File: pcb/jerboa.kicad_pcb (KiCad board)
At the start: 2 copper layers, 53.6 x 134.2 mm, 89 parts, among them IC1 SL18860DC, IC2 MAX-M8Q, IC3 Si4460, J1 CONN_01x02, J2 CONN_01x03, J3 CONN_01x02, J4 CONN_01x02, P1 SWD_TC, P2 144MHz, P3 434MHz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

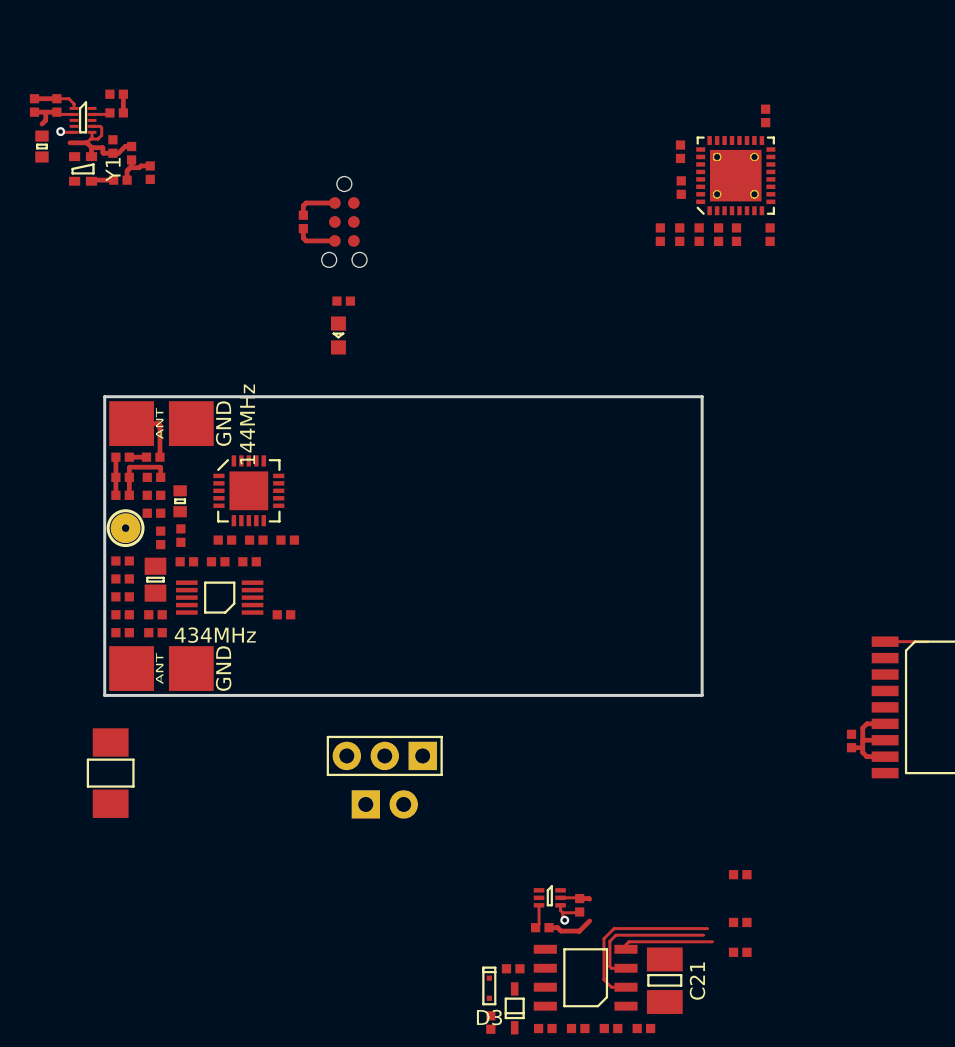
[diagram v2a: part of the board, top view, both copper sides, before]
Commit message: WIP: more pcb layout, add rx stuff again
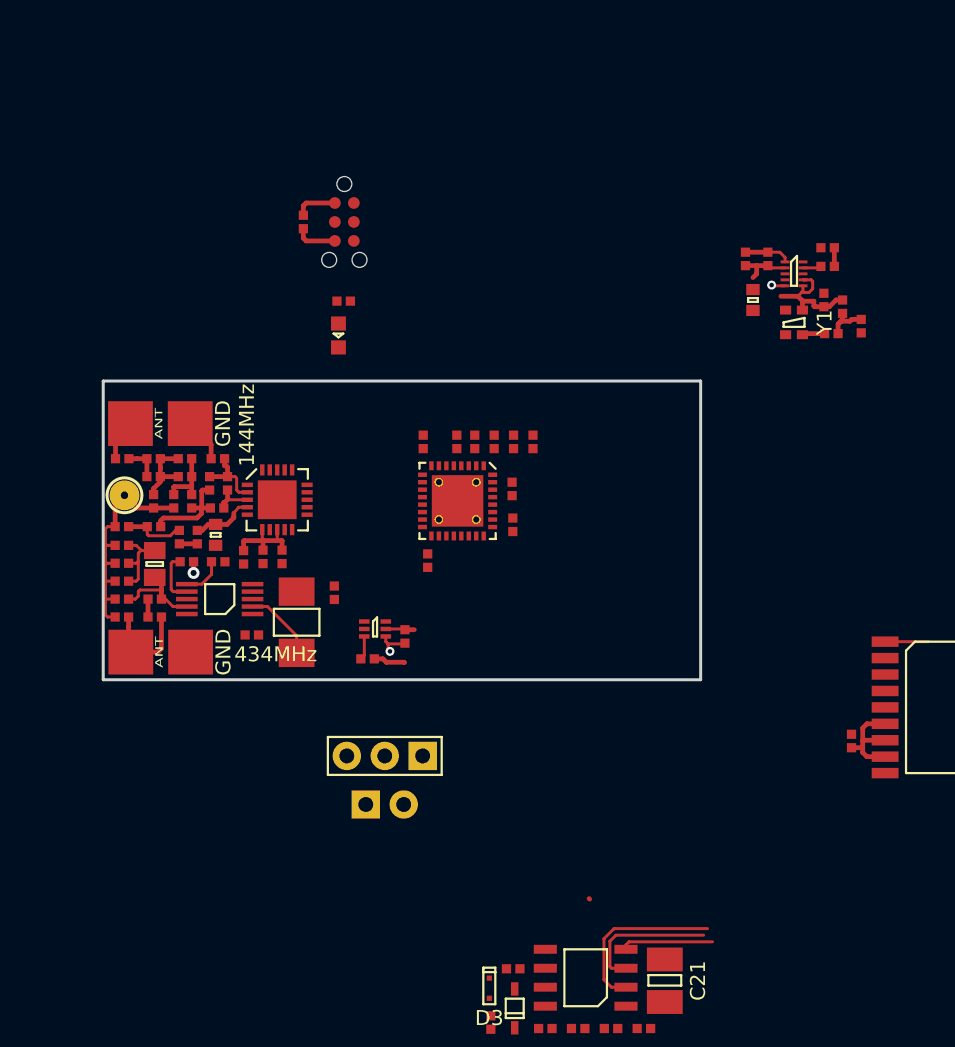
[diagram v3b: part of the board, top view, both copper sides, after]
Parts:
- added CR1: 12pF, agg:0402, F.Cu at (42.6, 84.2)
- added CR2: 6.2pF, agg:0402, F.Cu at (42.5, 87.5)
- added LR1: 220nH, agg:0402, F.Cu at (43.2, 85.8)
- added LR2: 150nH, agg:0402, F.Cu at (42.0, 85.8)
- moved CM3 49.5 mm to (38.3, 87.0), turned to 270 degrees
- moved CP2 49.3 mm to (38.3, 85.3), turned to 180 degrees
- moved C1 48.7 mm to (83.2, 73.5)
- moved C2 48.7 mm to (83.7, 75.8)
- moved C3 48.7 mm to (77.9, 70.8)
- moved C4 48.7 mm to (79.4, 70.8)
- moved IC1 48.7 mm to (81.2, 71.8)
- moved R1 48.7 mm to (84.4, 74.0)
- moved R2 48.7 mm to (85.7, 75.3)
- moved R3 48.7 mm to (78.4, 73.5)
- moved R4 48.7 mm to (83.4, 71.3)
- moved R5 48.7 mm to (83.4, 70.0)
- moved Y1 48.7 mm to (81.2, 75.0)
- moved CM2 45.4 mm to (39.6, 87.0), turned to 270 degrees
- moved C6 37.4 mm to (56.6, 91.0), turned to 90 degrees
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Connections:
- IC3 pad 2: /radio/RADIO_RXn -> /radio/RADIO_RXp
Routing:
- net GND: track 20.7 -> 40.2 mm, vias 2 -> 3
- net Net-(C30-Pad1): track 0.00 -> 8.33 mm
- net Net-(CR2-Pad2): track 0.00 -> 6.65 mm
- net Net-(C27-Pad2): track 0.00 -> 6.18 mm
- net Net-(C29-Pad1): track 0.00 -> 5.31 mm
- net 3v3: track 27.1 -> 32.1 mm
- net Net-(C22-Pad2): track 0.00 -> 4.91 mm
- net /radio/RADIO_RXp: track 0.00 -> 4.77 mm
- net /radio/RADIO_TX: track 0.00 -> 4.19 mm
- net Net-(CM1-Pad1): track 0.00 -> 4.10 mm
- net /MICRF_EN: track 0.00 -> 3.52 mm
- net Net-(R17-Pad1): track 0.00 -> 2.77 mm
- net /radio/RADIO_RXn: track 0.00 -> 2.67 mm
- net Net-(CM3-Pad1): track 2.55 -> 4.99 mm
- net Net-(CC2-Pad2): track 4.10 -> 2.76 mm
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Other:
- outline, holes or cut-outs redrawn

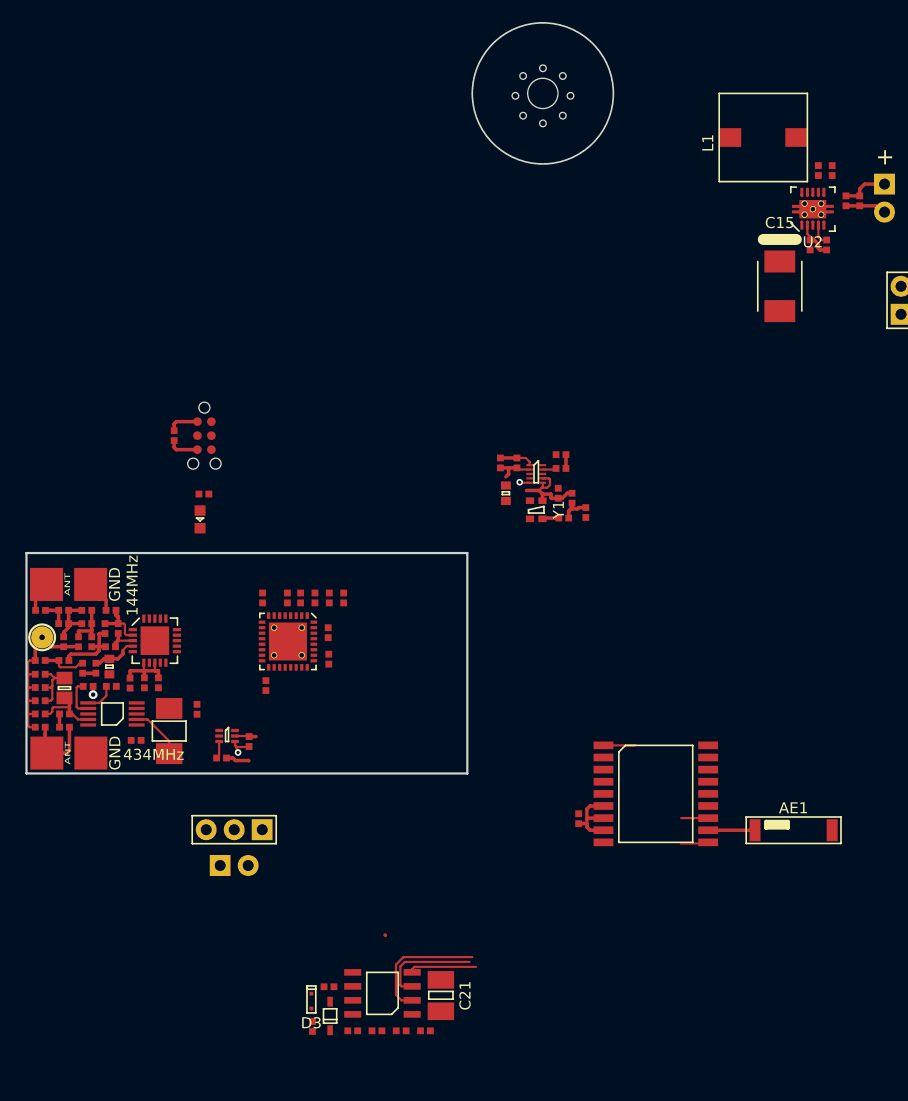
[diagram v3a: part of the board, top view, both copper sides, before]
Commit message: WIP: add clock circuitry to pcb
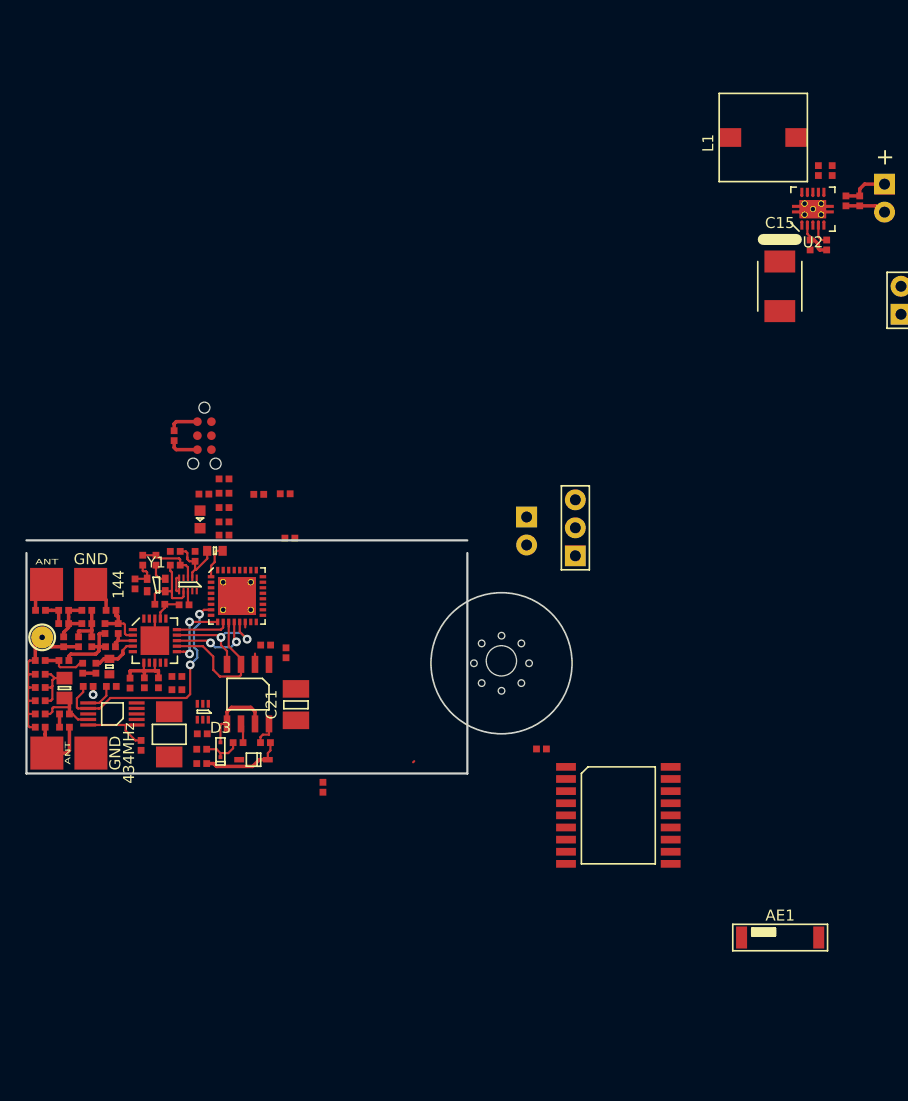
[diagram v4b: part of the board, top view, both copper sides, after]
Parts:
- P2: value 144MHz -> 144
- moved X1 51.6 mm to (78.0, 89.0)
- moved J2 41.3 mm to (84.7, 76.7), turned to 90 degrees
- moved J4 40.3 mm to (80.3, 77.0), turned to 270 degrees
- moved R1 39.4 mm to (45.5, 79.6), turned to 90 degrees
- moved C1 39.3 mm to (44.8, 81.8), turned to 90 degrees
- moved R5 38.8 mm to (47.0, 83.6)
- moved R2 37.6 mm to (48.4, 80.0), turned to 180 degrees
- moved C2 37.2 mm to (46.6, 79.6), turned to 90 degrees
- moved R13 37.1 mm to (56.6, 87.3)
- moved C20 36.6 mm to (58.5, 88.0), turned to 90 degrees
- moved R4 36.4 mm to (49.2, 83.7), turned to 180 degrees
- moved Y1 35.1 mm to (46.7, 81.8), turned to 0 degrees
- moved IC1 33.2 mm to (49.5, 81.8), turned to 270 degrees
- moved C3 30.6 mm to (48.4, 78.8), turned to 0 degrees
- moved C4 30.4 mm to (50.2, 79.2)
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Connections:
- IC1 pad 10: Net-(IC1-Pad10) -> /MCU_CLK
- IC1 pad 5: GND -> 3v3
- IC1 pad 7: 3v3 -> GND
- IC1 pad 8: /MCU_CLK -> Net-(IC1-Pad8)
- R4 pad 1: Net-(IC1-Pad9) -> Net-(IC1-Pad8)
- U1 pad 15: /MICRF_EN -> Net-(U1-Pad15)
- U1 pad 25: Net-(U1-Pad25) -> /LOW_BATT
- U1 pad 7: /LOW_BATT -> /MICRF_EN
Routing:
- net /MICRF_EN: track 3.52 -> 22.2 mm, vias 0 -> 2
- net /DAC_NCS: track 12.3 -> 1.47 mm
- net /MCU_MISO: track 0.00 -> 7.74 mm, vias 0 -> 2
- net Net-(C22-Pad1): track 0.00 -> 7.56 mm
- net /MCU_nIRQ_TO_RADIO: track 0.00 -> 6.70 mm, vias 0 -> 2
- net 3v3: track 32.1 -> 26.4 mm
- net Net-(C22-Pad2): track 4.91 -> 0.00 mm
- net /SI4460_NSS: track 0.00 -> 4.78 mm
- net /MCU_MOSI: track 6.65 -> 11.4 mm, vias 0 -> 2
- net Net-(AE1-Pad2): track 4.25 -> 0.00 mm
- net Net-(C23-Pad1): track 0.00 -> 3.61 mm
- net /MCU_SCK: track 9.74 -> 13.0 mm
- net Net-(C2-Pad2): track 2.99 -> 5.71 mm
- net GND: track 40.2 -> 42.7 mm, vias 3 -> 1
- net /radio/COARSE: track 0.00 -> 2.35 mm
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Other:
- board size 53.6 x 134.2 mm -> 49.8 x 87.2 mm

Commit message: WIP: attempt at routing spi
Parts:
- moved C6 32.1 mm to (54.8, 79.0), turned to 270 degrees
- moved C11 21.7 mm to (67.2, 78.9)
- moved R7 17.8 mm to (51.5, 90.8), turned to 90 degrees
- moved P1 16.4 mm to (63.0, 79.7), turned to 180 degrees
- moved IC2 16.0 mm to (101.2, 92.8)
- moved D1 15.2 mm to (49.7, 60.7)
- moved R6 15.2 mm to (50.0, 58.4)
- moved R9 15.1 mm to (44.9, 83.6), turned to 0 degrees
- moved C9 14.1 mm to (60.5, 85.3), turned to 180 degrees
- moved C7 11.6 mm to (51.4, 83.7)
- moved C8 7.72 mm to (51.4, 84.9)
- moved C10 6.45 mm to (51.9, 82.5)
- moved C5 4.30 mm to (53.6, 79.0), turned to 270 degrees
- moved U1 2.46 mm to (56.5, 83.0)
- moved R1 2.42 mm to (47.7, 80.5)
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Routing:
- net 3v3: track 26.4 -> 59.6 mm, vias 0 -> 2
- net /MCU_SHUTDOWN_TO_RADIO: track 0.00 -> 12.6 mm, vias 0 -> 2
- net /I2C_SCL: track 0.00 -> 11.6 mm
- net /I2C_SDA: track 0.00 -> 10.2 mm
- net /MCU_MOSI: track 11.4 -> 18.7 mm
- net /TMP_ALERT: track 0.07 -> 6.64 mm
- net /SWDIO: track 0.00 -> 6.13 mm
- net /MICRF_EN: track 22.2 -> 28.3 mm
- net /DAC_NCS: track 1.47 -> 7.02 mm
- net /SWCLK: track 0.00 -> 4.71 mm
- net Net-(C3-Pad2): track 5.88 -> 1.34 mm
- net /MCU_CLK: track 0.00 -> 4.18 mm
- net Net-(C24-Pad1): track 0.00 -> 2.70 mm
- net /SI4460_NSS: track 4.78 -> 7.43 mm
- net /MCU_SCK: track 13.0 -> 10.4 mm
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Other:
- board size 49.8 x 87.2 mm -> 49.8 x 87.5 mm

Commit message: WIP: more pcb layout
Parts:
- J3, J4: moved to F.Cu
- P2: value 144 -> 144MHz
- X1: footprint agg:M2.5_MOUNT -> agg:M2.5_HOLE
- moved J1 81.7 mm to (45.5, 100.2), turned to 0 degrees
- moved L1 54.0 mm to (68.1, 80.9), turned to 0 degrees
- moved J3 54.0 mm to (68.0, 76.9), turned to 180 degrees
- moved C13 53.1 mm to (67.0, 79.1), turned to 180 degrees
- moved C12 52.3 mm to (69.2, 79.1), turned to 0 degrees
- moved R10 50.3 mm to (73.3, 80.7), turned to 180 degrees
- moved R11 48.5 mm to (73.3, 79.4), turned to 0 degrees
- moved U2 47.6 mm to (74.6, 83.3), turned to 90 degrees
- moved R12 43.4 mm to (75.8, 80.7), turned to 180 degrees
- moved C14 41.5 mm to (75.8, 79.4), turned to 180 degrees
- moved C15 40.0 mm to (78.8, 84.2), turned to 180 degrees
- moved J2 37.9 mm to (46.8, 76.9), turned to 180 degrees
- moved IC2 33.0 mm to (68.2, 93.3)
- moved AE1 28.9 mm to (80.1, 96.7)
- moved J4 26.3 mm to (68.0, 100.2), turned to 0 degrees
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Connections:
- U1 pad 15: Net-(U1-Pad15) -> /SOLAR_CELL_VOLTAGE
- U1 pad 6: /SOLAR_CELL_VOLTAGE -> Net-(U1-Pad6)
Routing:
- net 3v3: track 59.6 -> 101.5 mm
- net Net-(C12-Pad1): track 4.31 -> 36.2 mm
- net /GPS_~RESET: track 0.00 -> 17.0 mm, vias 0 -> 2
- net GND: track 42.6 -> 59.1 mm, vias 3 -> 11
- net /TX_GPS_from_MCU: track 0.00 -> 10.8 mm
- net /RX_GPS_from_MCU: track 0.00 -> 10.2 mm
- net /I2C_SCL: track 11.6 -> 2.37 mm
- net /I2C_SDA: track 10.2 -> 2.77 mm
- net Net-(L1-Pad2): track 0.00 -> 6.18 mm
- net /SWDIO: track 6.13 -> 0.00 mm
- net Net-(C22-Pad2): track 0.00 -> 5.44 mm
- net /MICRF_EN: track 28.3 -> 23.2 mm, vias 2 -> 4
- net /SWCLK: track 4.71 -> 0.00 mm
- net Net-(R10-Pad2): track 0.00 -> 4.19 mm
- net Net-(AE1-Pad2): track 0.00 -> 3.70 mm
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- added copper zone on B.Cu, net GND
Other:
- board size 49.8 x 87.5 mm -> 50 x 118.1 mm
- board text added: "-"
